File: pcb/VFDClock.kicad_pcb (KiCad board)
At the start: 2 copper layers, 96.5 x 86.4 mm, 50 parts, among them J3 USB_C_Receptacle_USB2.0_16P, SW1 SW_SPST, SW2 SW_SPST, U1 TBD62783AFWG, U10 IP4234CZ6, U11 TXS0101DBV, U2 ESP32-S3-WROOM-1, U3 TBD62783AFNG, U4 SN74HC595PWR, U5 AMS1117-3.3, U6 BQ32000, U7 AMS1117-1.5, U8 DHT11, U9 APDS-9301

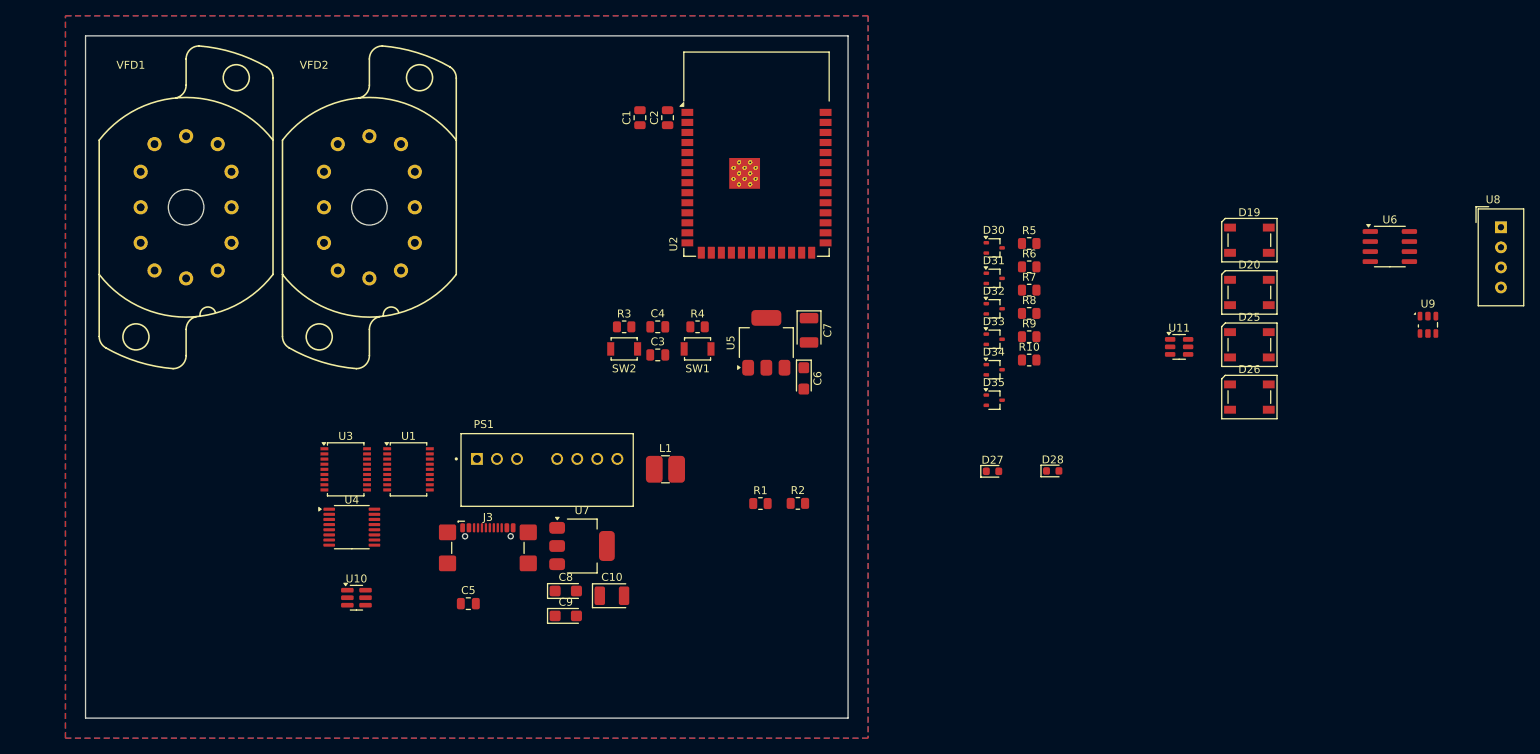
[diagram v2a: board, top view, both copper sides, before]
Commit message: Added footprints
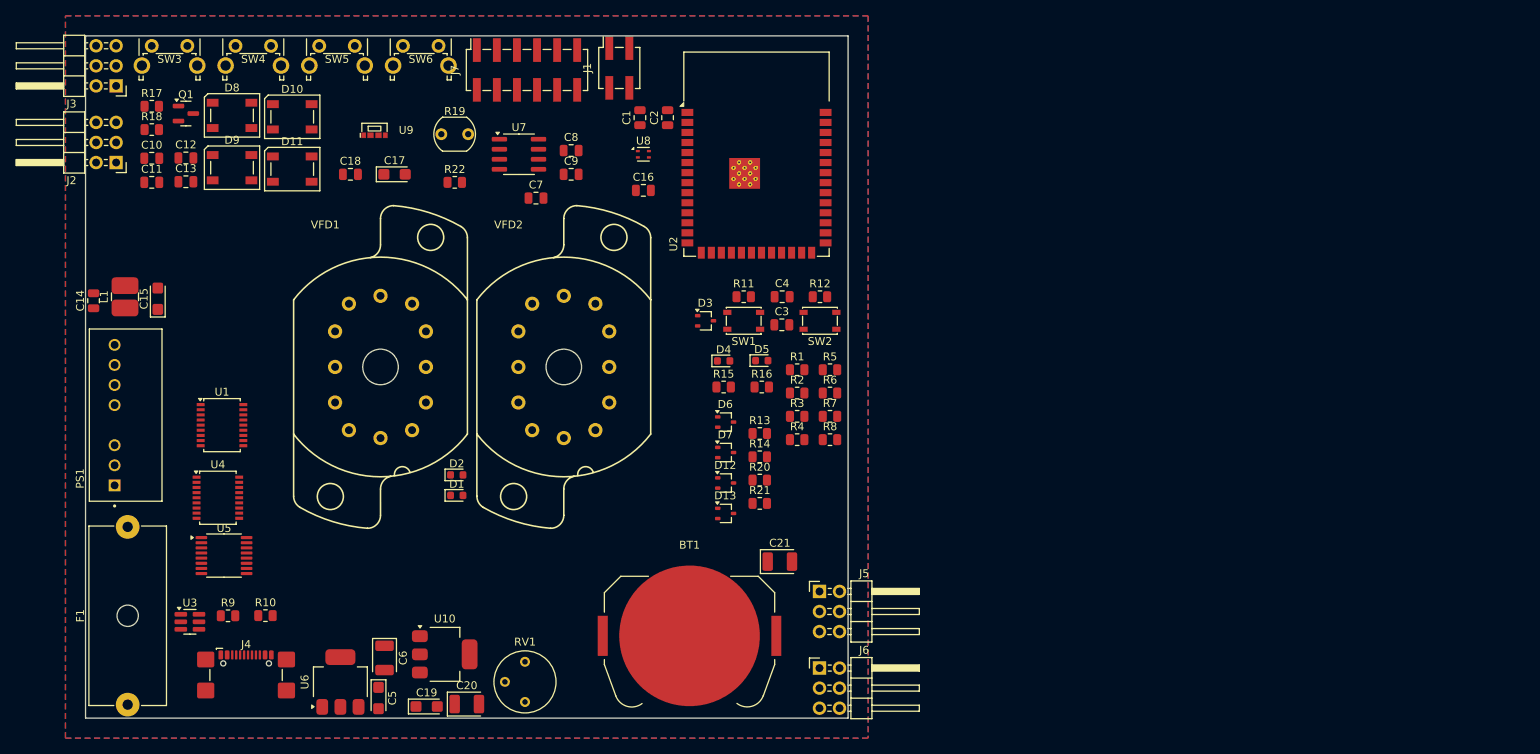
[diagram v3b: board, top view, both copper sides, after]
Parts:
- removed D35: 1PS70SB84, Package_TO_SOT_SMD:SOT-323_SC-70
- removed the SW1 at (161.3, 90.4)
- removed U11: TXS0101DBV, Package_TO_SOT_SMD:SOT-23-6
- removed the U6 at (248.9, 77.5)
- added BT1: CR2032, Battery:BatteryHolder_Keystone_3034_1x20mm, F.Cu at (160.3, 126.7)
- added C10: 100n, Capacitor_SMD:C_0805_2012Metric, F.Cu at (92.2, 66.3)
- added C11: 100n, Capacitor_SMD:C_0805_2012Metric, F.Cu at (92.2, 69.3)
- added C12: 100n, Capacitor_SMD:C_0805_2012Metric, F.Cu at (96.5, 66.3)
- added C13: 100n, Capacitor_SMD:C_0805_2012Metric, F.Cu at (96.5, 69.3)
- added C16: 100n, Capacitor_SMD:C_0805_2012Metric, F.Cu at (154.4, 70.4)
- added C17: 10u, Capacitor_Tantalum_SMD:CP_EIA-3216-18_Kemet-A, F.Cu at (122.9, 68.3)
- added C18: 100n, Capacitor_SMD:C_0805_2012Metric, F.Cu at (117.3, 68.3)
- added C21: 22u, Capacitor_Tantalum_SMD:CP_EIA-3528-15_AVX-H, F.Cu at (171.7, 117.3)
- added C7: 1n, Capacitor_SMD:C_0805_2012Metric, F.Cu at (140.8, 71.3)
- added C8: 100n, Capacitor_SMD:C_0805_2012Metric, F.Cu at (145.3, 65.3)
- added C9: 100n, Capacitor_SMD:C_0805_2012Metric, F.Cu at (145.3, 68.3)
- added D1: XGD10603MR, Diode_SMD:D_0603_1608Metric, F.Cu at (130.8, 109.0)
- added D2: XGD10603MR, Diode_SMD:D_0603_1608Metric, F.Cu at (130.8, 106.4)
- added F1: 3,5 A, Fuse:Fuseholder_Cylinder-5x20mm_Schurter_0031_8201_Horizontal_Open, F.Cu at (89.2, 135.5)
- added J1: Conn_01x04_Socket, Connector_PinSocket_2.54mm:PinSocket_2x02_P2.54mm_Vertical_SMD, F.Cu at (151.4, 54.9)
- added J2: L_SIG_CONN, Connector_PinHeader_2.54mm:PinHeader_2x03_P2.54mm_Horizontal, F.Cu at (87.7, 66.8)
- added J3: L_PWR_CONN, Connector_PinHeader_2.54mm:PinHeader_2x03_P2.54mm_Horizontal, F.Cu at (87.7, 57.1)
- added J5: R_SIG_CONN, Connector_PinHeader_2.54mm:PinHeader_2x03_P2.54mm_Horizontal, F.Cu at (176.7, 121.1)
- added J6: R_PWR_CONN, Connector_PinHeader_2.54mm:PinHeader_2x03_P2.54mm_Horizontal, F.Cu at (176.7, 130.8)
- added J7: Conn_02x06_Top_Bottom, Connector_PinSocket_2.54mm:PinSocket_2x06_P2.54mm_Vertical_SMD, F.Cu at (139.7, 55.1)
- added Q1: BSS138, Package_TO_SOT_SMD:SOT-23, F.Cu at (96.5, 60.6)
- added R1: 4k7, Resistor_SMD:R_0805_2012Metric, F.Cu at (173.9, 93.1)
- added R17: 10k, Resistor_SMD:R_0805_2012Metric, F.Cu at (92.2, 59.7)
- added R18: 10k, Resistor_SMD:R_0805_2012Metric, F.Cu at (92.2, 62.7)
- added R19: R_Photo, OptoDevice:R_LDR_5.1x4.3mm_P3.4mm_Vertical, F.Cu at (128.9, 63.2)
- added R2: 4k7, Resistor_SMD:R_0805_2012Metric, F.Cu at (173.9, 96.0)
- added R22: 10k, Resistor_SMD:R_0805_2012Metric, F.Cu at (130.6, 69.3)
- added R3: 4k7, Resistor_SMD:R_0805_2012Metric, F.Cu at (173.9, 99.0)
- added R4: 4k7, Resistor_SMD:R_0805_2012Metric, F.Cu at (173.9, 101.9)
- added R5: 4k7, Resistor_SMD:R_0805_2012Metric, F.Cu at (178.1, 93.1)
- added R6: 4k7, Resistor_SMD:R_0805_2012Metric, F.Cu at (178.1, 96.0)
- added R7: 4k7, Resistor_SMD:R_0805_2012Metric, F.Cu at (178.1, 99.0)
- added R8: 4k7, Resistor_SMD:R_0805_2012Metric, F.Cu at (178.1, 101.9)
- added RV1: 10, Potentiometer_THT:Potentiometer_Bourns_3339P_Vertical, F.Cu at (139.4, 135.1)
- added SW2: SW_SPST, Button_Switch_SMD:SW_SPST_PTS810, F.Cu at (176.8, 86.9)
- added SW3: SW_SPST, Button_Switch_THT:SW_Tactile_SPST_Angled_PTS645Vx83-2LFS, F.Cu at (92.2, 52.1)
- added SW4: SW_SPST, Button_Switch_THT:SW_Tactile_SPST_Angled_PTS645Vx83-2LFS, F.Cu at (102.8, 52.1)
- added SW5: SW_SPST, Button_Switch_THT:SW_Tactile_SPST_Angled_PTS645Vx83-2LFS, F.Cu at (113.4, 52.1)
- added SW6: SW_SPST, Button_Switch_THT:SW_Tactile_SPST_Angled_PTS645Vx83-2LFS, F.Cu at (124.0, 52.1)
- added U7: DS3231MZ+TRL, Package_SO:SOIC-8_3.9x4.9mm_P1.27mm, F.Cu at (138.7, 65.8)
- SW1: renamed from SW2; footprint Button_Switch_SMD:SW_SPST_B3U-1000P -> Button_Switch_SMD:SW_SPST_PTS810
- U8: value DHT11 -> SHT45-AD1B-R2; footprint Sensor:Aosong_DHT11_5.5x12.0_P2.54mm -> Sensor_Humidity:Sensirion_DFN-4_1.5x1.5mm_P0.8mm_SHT4x_NoCentralPad
- U9: value APDS-9301 -> VEML3235SL; footprint OptoDevice:Broadcom_APDS-9301 -> VFDClock_custom_lib:VEML3235SL_Vertical
- moved U9 135.6 mm to (120.4, 62.7)
- moved D8 129.7 mm to (102.4, 60.9)
- moved D9 129.7 mm to (102.4, 67.5)
- moved D10 124.5 mm to (110.0, 61.0)
- moved D11 124.5 mm to (110.0, 67.7)
- moved U8 108.9 mm to (154.4, 65.8)
- moved L1 71.8 mm to (88.8, 83.8), turned to 90 degrees
- moved U6 68.9 mm to (116.1, 132.6)
- moved R10 68.9 mm to (106.6, 124.2)
- moved R9 68.9 mm to (101.9, 124.2)
- moved C6 67.9 mm to (121.7, 129.5)
- moved C5 67.4 mm to (120.9, 134.6)
- moved C15 63.5 mm to (93.0, 84.1), turned to 90 degrees
- moved C14 61.0 mm to (84.8, 84.3), turned to 90 degrees
- moved PS1 53.8 mm to (88.9, 98.8), turned to 90 degrees
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- renumbered C5 to C14, C8 to C15, C9 to C19, C10 to C20, C6 to C5, C7 to C6, D25 to D10, D26 to D11, D33 to D12, D34 to D13, D30 to D3, D27 to D4, D28 to D5, D31 to D6, D32 to D7, D19 to D8, D20 to D9, J3 to J4, R2 to R10, R3 to R11, R4 to R12, R5 to R13, R6 to R14, R9 to R15, R10 to R16, R7 to R20, R8 to R21, R1 to R9, U7 to U10, U10 to U3, U3 to U4, U4 to U5, U5 to U6
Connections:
- U2 pad 15: unconnected-(U2-IO3-Pad15) -> /GPIO3
- U2 pad 25: unconnected-(U2-IO48-Pad25) -> /GPIO48
- U2 pad 32: /TEMP_DATA -> /GPIO39
- U2 pad 33: unconnected-(U2-IO40-Pad33) -> /GPIO40
- U2 pad 34: unconnected-(U2-IO41-Pad34) -> /GPIO41
- U2 pad 35: unconnected-(U2-IO42-Pad35) -> /GPIO42
- U2 pad 36: unconnected-(U2-RXD0-Pad36) -> Net-(J1-Pin_3)
- U2 pad 37: unconnected-(U2-TXD0-Pad37) -> Net-(J1-Pin_2)
- U2 pad 8: /RTC_SCL -> /Uphoto
- U2 pad 9: /RTC_SDA -> /GPIO16
- U3 pad 5: +5V -> Net-(U3-VP)
- U8 pad 1: +3V3 -> /SDA
- U8 pad 2: /TEMP_DATA -> /SCL
- U8 pad 3: unconnected-(U8-NC-Pad3) -> +3V3
- U9 pad 3: GND -> /SCL
- U9 pad 4: /SCL -> /SDA

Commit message: Added custom USB-C footprint
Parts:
- C10, C11, C12, C13, D10, D11, D8, D9, Q1, R17, R18: moved to B.Cu
- J4: footprint Connector_USB:USB_C_Receptacle_GCT_USB4110 -> VFDClock_custom_lib:CUI_UJ20-C-V-C-2-SMT-TR
- VFD1, VFD2: footprint Vacuum_Tubes:PL31-A_P_Socket -> VFDClock_custom_lib:PL31-A_P_Socket; moved to B.Cu
- moved D12 158.5 mm to (21.8, 39.0)
- moved D13 158.5 mm to (21.8, 42.8)
- moved D6 158.5 mm to (21.8, 31.2)
- moved D7 158.5 mm to (21.8, 35.1)
- moved R13 158.5 mm to (26.2, 32.7)
- moved R14 158.5 mm to (26.2, 35.6)
- moved R20 158.5 mm to (26.2, 38.6)
- moved R21 158.5 mm to (26.2, 41.5)
- moved C18 115.0 mm to (232.2, 74.2)
- moved U9 115.0 mm to (235.3, 68.6)
- moved C17 115.0 mm to (237.8, 74.2)
- moved C7 115.0 mm to (255.7, 77.2)
- moved R19 115.0 mm to (243.7, 69.1)
- moved R22 115.0 mm to (245.4, 75.2)
- moved U7 115.0 mm to (253.6, 71.6)
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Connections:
- VFD1 pad 9: unconnected-(VFD1-Pad9) -> (no net)
- VFD2 pad 9: unconnected-(VFD2-Pad9) -> (no net)
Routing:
- net Net-(J4-D+-PadA6): track 0.00 -> 1.78 mm
- net Net-(J4-D--PadA7): track 0.00 -> 1.77 mm
- added copper zone on B.Cu, net +5V
- added copper zone on F.Cu, net +5V
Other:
- board size 96.5 x 86.4 mm -> 70 x 90 mm

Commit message: Initial component placement
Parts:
- VFD1, VFD2: footprint VFDClock_custom_lib:PL31-A_P_Socket -> Connector_PinSocket_2.54mm:PinSocket_1x12_P2.54mm_Vertical
- moved D12 146.6 mm to (165.6, 67.7)
- moved D13 146.6 mm to (165.6, 71.6)
- moved R20 146.6 mm to (169.9, 67.3)
- moved R21 146.6 mm to (169.9, 70.3)
- moved SW5 94.7 mm to (145.2, 67.5)
- moved SW6 93.8 mm to (154.8, 67.5)
- moved U2 85.1 mm to (132.1, 77.6), turned to 0 degrees
- moved D6 82.3 mm to (95.7, 67.5)
- moved D7 82.3 mm to (95.7, 71.4)
- moved R13 82.3 mm to (100.0, 69.0)
- moved R14 82.3 mm to (100.0, 71.9)
- moved C2 77.5 mm to (120.1, 74.0)
- moved SW3 76.9 mm to (104.9, 67.5)
- moved C1 76.1 mm to (118.1, 74.0)
- moved SW4 75.9 mm to (114.5, 67.5)
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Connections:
- J2 pad 2: /GRID_L2 -> /SRCLK
- J2 pad 3: /SER_LEFT -> /GRID_L2
- J2 pad 4: /SRCLK -> //SRCLR
- J2 pad 5: //SRCLR -> /SER_LEFT
- J3 pad 2: +5V -> GND
- J3 pad 5: GND -> +5V
- J5 pad 2: /GRID_R2 -> /SRCLK
- J5 pad 3: /SER_RIGHT -> /GRID_R2
- J5 pad 4: /SRCLK -> //SRCLR
- J5 pad 5: //SRCLR -> /SER_RIGHT
- J6 pad 2: +5V -> GND
- J6 pad 5: GND -> +5V
- J7 pad 10: /GPIO48 -> GND
- J7 pad 2: /GPIO3 -> +5V
- J7 pad 3: /GPIO16 -> /GPIO3
- J7 pad 4: /GPIO39 -> /GPIO41
- J7 pad 5: /GPIO40 -> /GPIO16
- J7 pad 6: GND -> /GPIO42
- J7 pad 7: +5V -> /GPIO39
- J7 pad 8: /GPIO41 -> /GPIO48
- J7 pad 9: /GPIO42 -> /GPIO40
- U1 pad 1: /DRIVER_L1 -> /DRIVER_R2
- U1 pad 13: /GRID_R2 -> /GRID_L1
- U1 pad 14: /GRID_R1 -> /GRID_L2
- U1 pad 15: Net-(D2-A2) -> Net-(D1-A2)
- U1 pad 16: Net-(D1-A2) -> Net-(D2-A2)
- U1 pad 17: /GRID_L2 -> /GRID_R1
- U1 pad 18: /GRID_L1 -> /GRID_R2
- U1 pad 2: /DRIVER_L2 -> /DRIVER_R1
- U1 pad 3: /DRIVER_M1 -> /DRIVER_M2
- U1 pad 4: /DRIVER_M2 -> /DRIVER_M1
- U1 pad 5: /DRIVER_R1 -> /DRIVER_L2
- U1 pad 6: /DRIVER_R2 -> /DRIVER_L1
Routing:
- net Net-(D1-A2): track 0.00 -> 31.4 mm
- net Net-(D2-A2): track 0.00 -> 29.6 mm
- net Net-(U4-O7): track 0.00 -> 22.4 mm, vias 0 -> 1
- net Net-(U4-I2): track 0.00 -> 22.1 mm, vias 0 -> 2
- net Net-(U4-I3): track 0.00 -> 20.8 mm, vias 0 -> 2
- net Net-(U4-O8): track 0.00 -> 20.6 mm
- net Net-(U4-O6): track 0.00 -> 19.8 mm
- net Net-(U4-I4): track 0.00 -> 19.1 mm, vias 0 -> 2
- net Net-(U4-O4): track 0.00 -> 19.0 mm
- net Net-(U4-O5): track 0.00 -> 18.4 mm, vias 0 -> 1
- net Net-(U4-O3): track 0.00 -> 17.0 mm
- net Net-(U4-I5): track 0.00 -> 16.3 mm, vias 0 -> 2
- net Net-(U4-I6): track 0.00 -> 14.5 mm
- net Net-(U4-I7): track 0.00 -> 12.8 mm
- net Net-(U4-O2): track 0.00 -> 11.5 mm
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- added copper zone on In1.Cu, net GND
- added copper zone on In2.Cu, net GND
- removed copper zone on F.Cu, net GND
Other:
- board size 70 x 90 mm -> 80 x 90 mm
- copper layers 2 -> 4

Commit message: Footprint placement progress
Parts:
- removed the C21 at (173.3, 153.9)
- removed the R3 at (217.6, 108.4)
- removed the R4 at (217.6, 111.4)
- BT1, C1, C16, C17, C18, C2, C3, C4, D12, D13, D6, D7, U8: moved to B.Cu
- D4: footprint Diode_SMD:D_0603_1608Metric -> LED_SMD:LED_0603_1608Metric
- R10: renamed from R12; moved to B.Cu
- R11: renamed from R13; moved to B.Cu
- R12: renamed from R14; moved to B.Cu
- R18: renamed from R20; moved to B.Cu
- R19: renamed from R21; moved to B.Cu
- R3: renamed from R5; moved to B.Cu
- R4: renamed from R6; moved to B.Cu
- R5: renamed from R7; moved to B.Cu
- R6: renamed from R8; moved to B.Cu
- R9: renamed from R11; moved to B.Cu
- U9: footprint VFDClock_custom_lib:VEML3235SL_Vertical -> VFDClock_custom_lib:VEML3235SL_Horizontal; moved to B.Cu
- moved R17 146.1 mm to (46.2, 124.0)
- moved R20 146.1 mm to (47.9, 130.1)
- moved U8 105.5 mm to (109.6, 97.4)
- moved C9 103.2 mm to (114.3, 102.1), turned to 180 degrees
- moved C16 102.6 mm to (112.3, 97.4), turned to -90 degrees
- moved C8 101.7 mm to (116.1, 109.5)
- moved R4 101.0 mm to (109.6, 99.4), turned to 180 degrees
- moved R3 101.0 mm to (109.6, 95.4), turned to 180 degrees
- moved C7 100.5 mm to (112.5, 109.5), turned to 180 degrees
- moved U7 96.6 mm to (114.3, 105.8)
- moved R10 92.3 mm to (116.8, 95.5), turned to 90 degrees
- moved SW2 90.6 mm to (117.8, 95.4), turned to 0 degrees
- moved C3 85.7 mm to (118.8, 99.2), turned to -90 degrees
- moved C4 84.9 mm to (120.8, 99.2), turned to -90 degrees
- moved R9 84.0 mm to (116.8, 99.2), turned to 90 degrees
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- renumbered C19 to C20, C20 to C21, R15 to R13, R16 to R14, R17 to R15, R18 to R16, R19 to R17, R22 to R20, R9 to R7, R10 to R8
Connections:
- J7 pad 5: /GPIO16 -> /GPIO8
- U2 pad 12: /BTN4 -> /GPIO8
- U2 pad 28: /SRCLK -> //SRCLR
- U2 pad 29: //SRCLR -> /SRCLK
- U2 pad 8: /Uphoto -> /BTN4
- U2 pad 9: /GPIO16 -> /Uphoto
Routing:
- net +3V3: track 0.00 -> 49.0 mm, vias 0 -> 8
- net /BTN4: track 0.00 -> 45.7 mm
- net /SCL: track 0.00 -> 37.5 mm, vias 0 -> 2
- net /SDA: track 0.00 -> 37.2 mm, vias 0 -> 2
- net /BTN3: track 0.00 -> 37.0 mm
- net /BOOT: track 0.00 -> 36.2 mm, vias 0 -> 1
- net /BTN1: track 0.00 -> 36.1 mm
- net /BTN2: track 0.00 -> 28.5 mm
- net GND: track 9.95 -> 37.2 mm, vias 2 -> 15
- net /SER_MID: track 0.00 -> 25.2 mm, vias 0 -> 2
- net /RCLK: track 4.29 -> 28.0 mm, vias 0 -> 2
- net /SRCLK: track 9.78 -> 32.1 mm, vias 0 -> 2
- net //SRCLR: track 7.04 -> 28.3 mm, vias 0 -> 2
- net /GPIO3: track 0.00 -> 20.9 mm, vias 0 -> 1
- net /SER_LEFT: track 4.27 -> 24.7 mm, vias 0 -> 2
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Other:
- board size 80 x 90 mm -> 80 x 52.7 mm
